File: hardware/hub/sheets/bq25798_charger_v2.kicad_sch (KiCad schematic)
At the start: 39 parts, among them J302 S2B-ZR, Q301 AO3400A, Q302 AO3400A, Q303 AO3400A, Q304 AO3400A, SW3 WAKE, U8 BQ25798RQMR

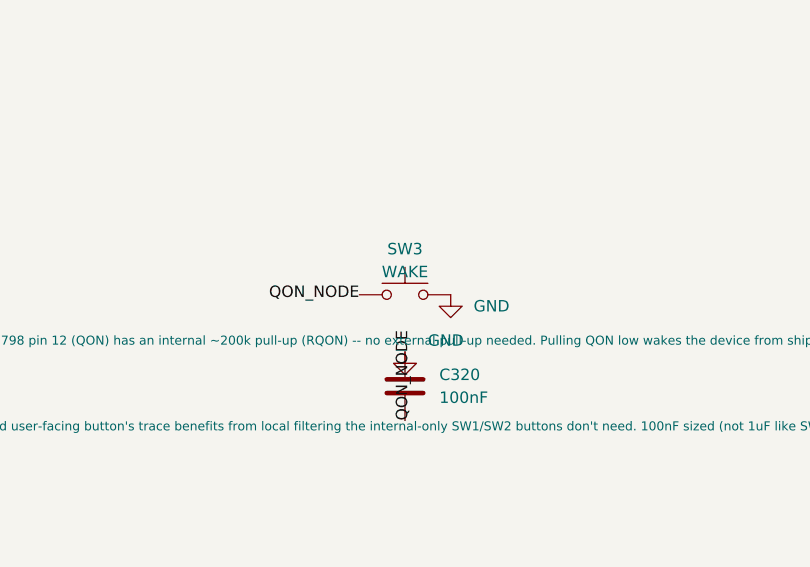
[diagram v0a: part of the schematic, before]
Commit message: Small labeling and placement tweaks to make the BOM selection during PCBA services more efficient
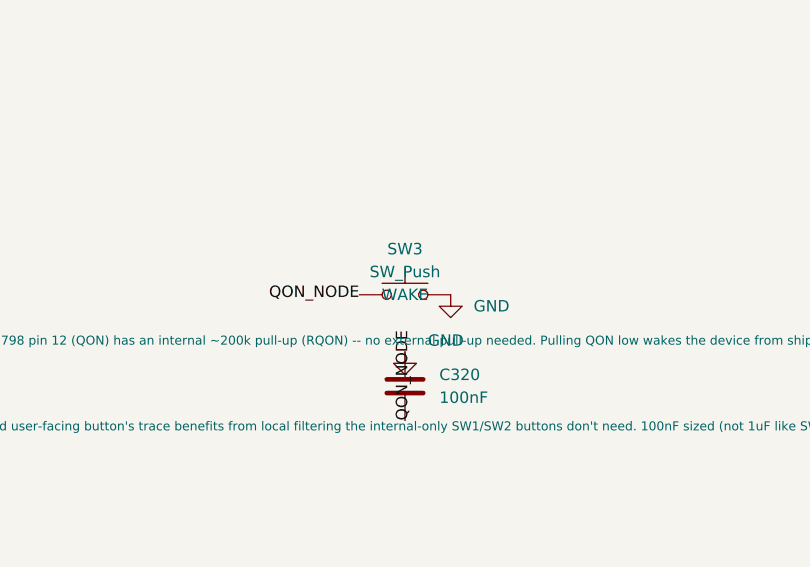
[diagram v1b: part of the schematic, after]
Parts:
- SW3: value WAKE -> SW_Push
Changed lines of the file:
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@@
 			)
 		)
-		(property "Value" "WAKE"
+		(property "Value" "SW_Push"
 			(at 445.77 213.36 0)
 			(show_name no)
@@
 			)
 		)
-		(property "Description" ""
+		(property "Description" "WAKE"
 			(at 445.77 215.9 0)
 			(show_name no)
